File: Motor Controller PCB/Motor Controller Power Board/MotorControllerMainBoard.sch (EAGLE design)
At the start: 58 parts, among them U1 CDBA340L-G

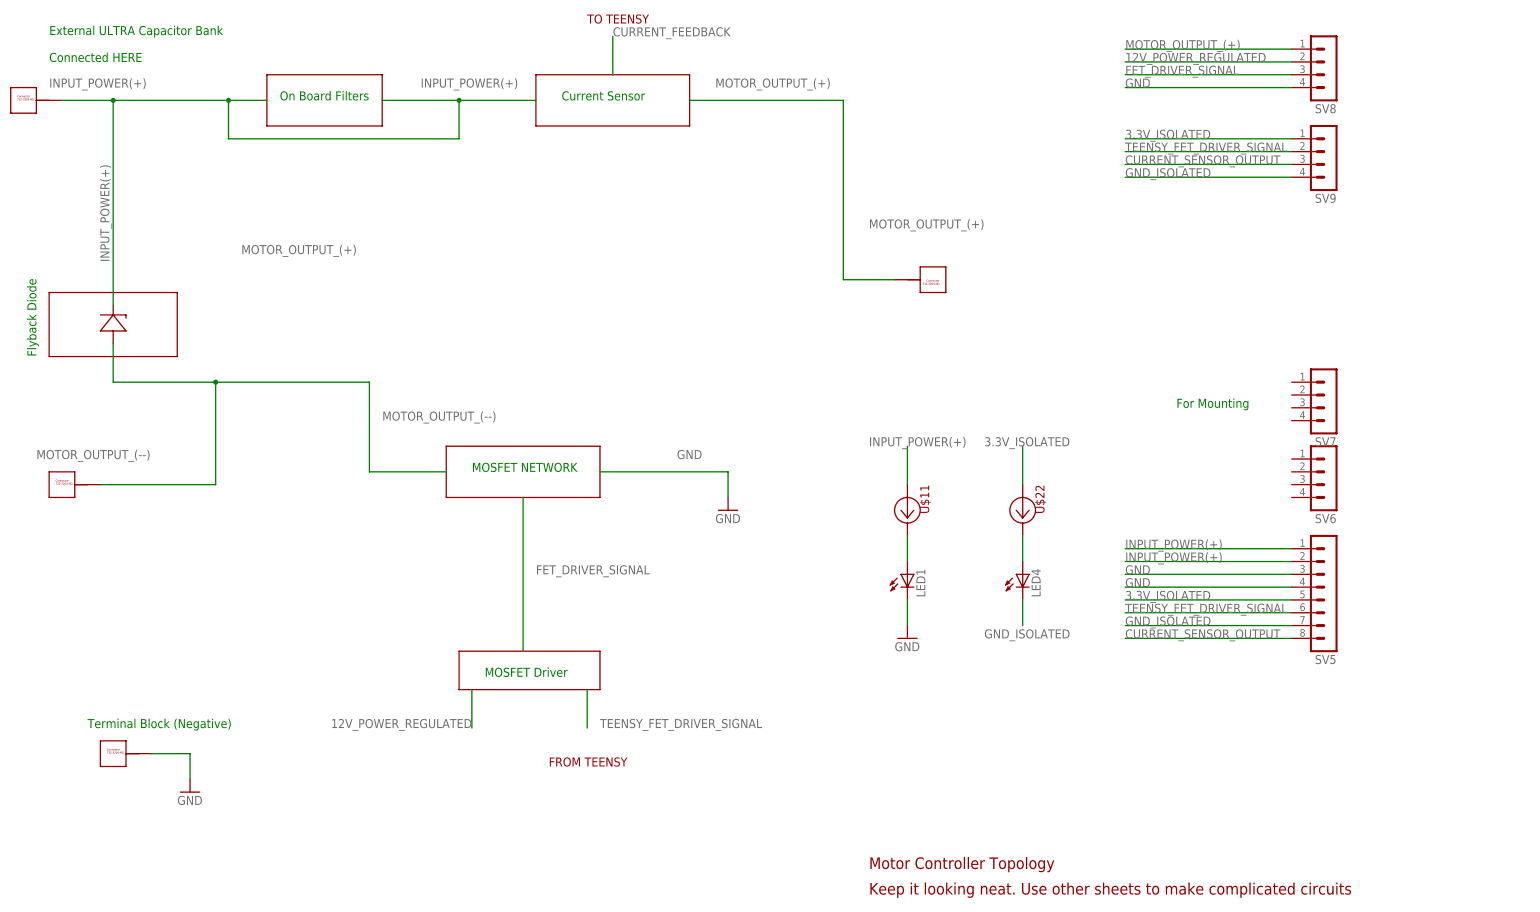
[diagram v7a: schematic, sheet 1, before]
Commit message: added heatsink for flyback diode
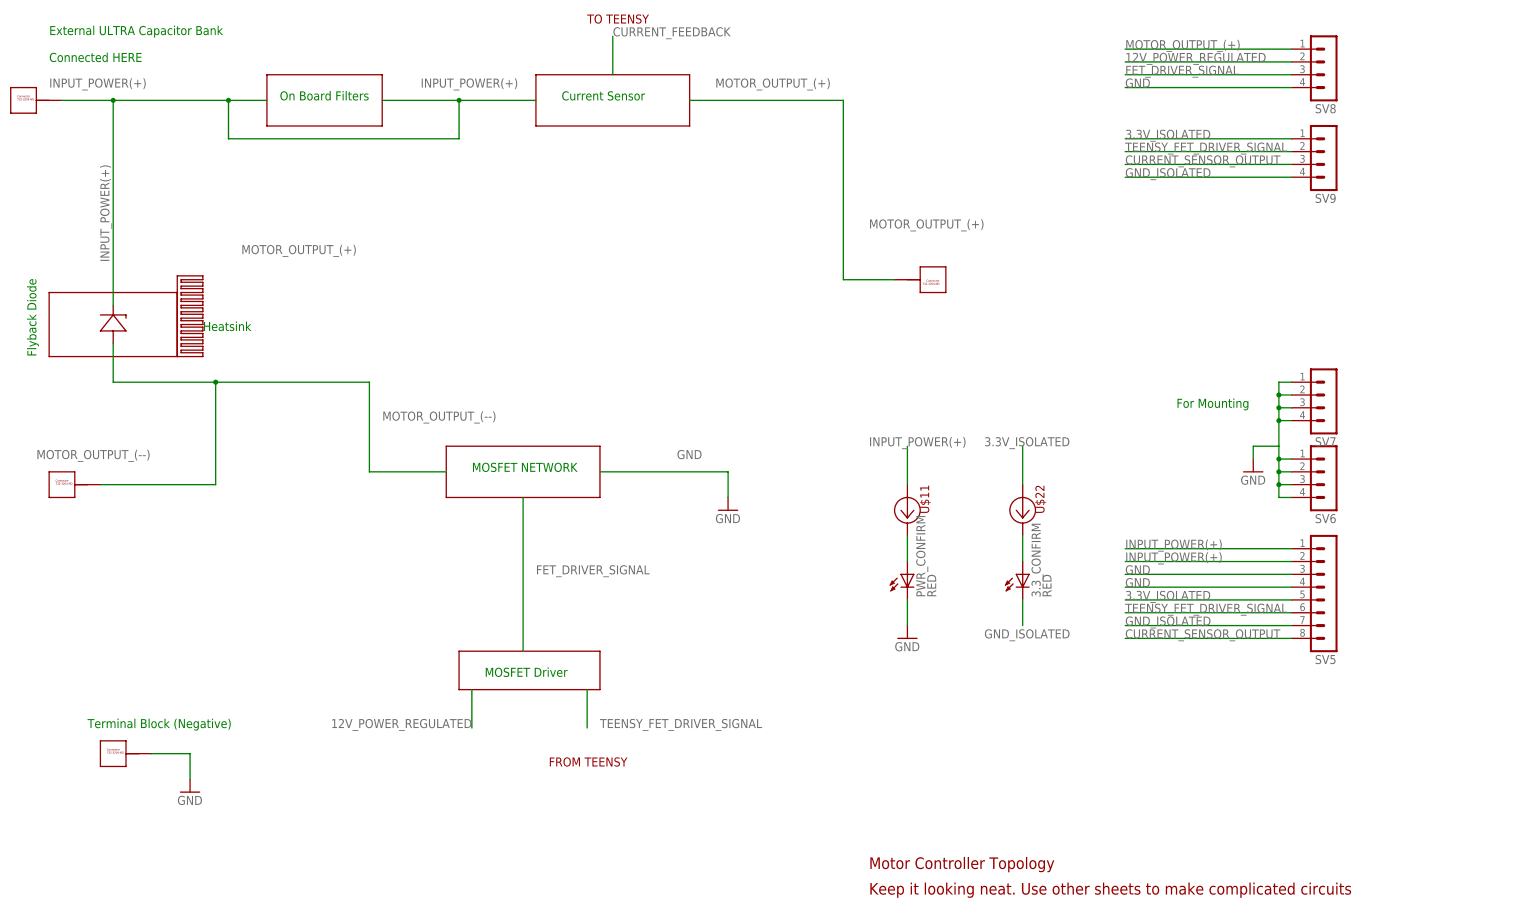
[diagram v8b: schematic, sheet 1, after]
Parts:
- added U$23: DA-T263-101E, MotorControllerEagleLibrary:DA-T263-101E
- 3.3_CONFIRM, PWR_CONFIRM: value (none) -> RED
- renumbered LED1 to PWR_CONFIRM, LED4 to 3.3_CONFIRM
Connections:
- net GND: now also SV6.1, SV6.2, SV6.3, SV6.4, SV7.1, SV7.2, SV7.3, SV7.4
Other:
- note added: "Heatsink"
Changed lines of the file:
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@@
 <?xml version="1.0" encoding="utf-8"?>
 <!DOCTYPE eagle SYSTEM "eagle.dtd">
-<eagle version="8.4.0">
+<eagle version="8.6.0">
 <drawing>
 <settings>
@@
 <part name="C8" library="MotorControllerEagleLibrary" deviceset="EEUFR1H221B" device=""/>
 <part name="U$11" library="MotorControllerEagleLibrary" deviceset="AL5809-20S1-7" device=""/>
-<part name="LED1" library="led" library_urn="urn:adsk.eagle:library:259" deviceset="LED" device="CHIPLED_1206" package3d_urn="urn:adsk.eagle:package:15823/1"/>
+<part name="PWR_CONFIRM" library="led" library_urn="urn:adsk.eagle:library:259" deviceset="LED" device="CHIPLED_1206" package3d_urn="urn:adsk.eagle:package:15823/2" value="RED"/>
 <part name="GND22" library="E-P-008-R1.2" deviceset="GND" device=""/>
 <part name="U$10" library="MotorControllerEagleLibrary" deviceset="EEU-FM1H102B" device=""/>
@@
 <part name="SV9" library="con-lstb" library_urn="urn:adsk.eagle:library:162" deviceset="MA04-1" device="" package3d_urn="urn:adsk.eagle:package:8337/1"/>
 <part name="U$22" library="MotorControllerEagleLibrary" deviceset="AL5809-20S1-7" device=""/>
-<part name="LED4" library="led" library_urn="urn:adsk.eagle:library:259" deviceset="LED" device="CHIPLED_1206" package3d_urn="urn:adsk.eagle:package:15823/1"/>
+<part name="3.3_CONFIRM" library="led" library_urn="urn:adsk.eagle:library:259" deviceset="LED" device="CHIPLED_1206" package3d_urn="urn:adsk.eagle:package:15823/2" value="RED"/>
+<part name="GND10" library="E-P-008-R1.2" deviceset="GND" device=""/>
+<part name="U$23" library="MotorControllerEagleLibrary" deviceset="DA-T263-101E" device=""/>
 </parts>
 <sheets>
@@
 <text x="20.32" y="58.42" size="1.778" layer="91">Terminal Block (Negative)</text>
 <text x="236.22" y="121.92" size="1.778" layer="91">For Mounting</text>
+<text x="43.18" y="137.16" size="1.778" layer="91">Heatsink</text>
 </plain>
 <instances>
@@
 <instance part="U$16" gate="G$1" x="15.24" y="106.68"/>
 <instance part="U$11" gate="G$1" x="182.88" y="101.6" rot="R180"/>
-<instance part="LED1" gate="G$1" x="182.88" y="88.9"/>
+<instance part="PWR_CONFIRM" gate="G$1" x="182.88" y="88.9"/>
 <instance part="GND22" gate="1" x="182.88" y="76.2"/>
 <instance part="SV5" gate="1" x="266.7" y="86.36" rot="R180"/>
@@
 <instance part="SV9" gate="1" x="266.7" y="170.18" rot="R180"/>
 <instance part="U$22" gate="G$1" x="205.74" y="101.6" rot="R180"/>
-<instance part="LED4" gate="G$1" x="205.74" y="88.9"/>
+<instance part="3.3_CONFIRM" gate="G$1" x="205.74" y="88.9"/>
+<instance part="GND10" gate="1" x="251.46" y="109.22"/>
+<instance part="U$23" gate="G$1" x="38.1" y="139.7" rot="R270"/>
 </instances>
 <busses>
@@
 </segment>
 <segment>
-<pinref part="LED1" gate="G$1" pin="C"/>
+<pinref part="PWR_CONFIRM" gate="G$1" pin="C"/>
 <wire x1="182.88" y1="83.82" x2="182.88" y2="78.74" width="0.1524" layer="91"/>
 <pinref part="GND22" gate="1" pin="GND"/>
@@
 <wire x1="259.08" y1="185.42" x2="226.06" y2="185.42" width="0.1524" layer="91"/>
 <label x="226.06" y="185.42" size="1.778" layer="95"/>
+</segment>
+<segment>
+<pinref part="SV7" gate="1" pin="1"/>
+<wire x1="259.08" y1="127" x2="256.54" y2="127" width="0.1524" layer="91"/>
+<wire x1="256.54" y1="127" x2="256.54" y2="124.46" width="0.1524" layer="91"/>
+<pinref part="SV7" gate="1" pin="4"/>
+<wire x1="256.54" y1="124.46" x2="256.54" y2="121.92" width="0.1524" layer="91"/>
+<wire x1="256.54" y1="121.92" x2="256.54" y2="119.38" width="0.1524" layer="91"/>
+<wire x1="256.54" y1="119.38" x2="259.08" y2="119.38" width="0.1524" layer="91"/>
+<pinref part="SV7" gate="1" pin="2"/>
+<wire x1="259.08" y1="124.46" x2="256.54" y2="124.46" width="0.1524" layer="91"/>
+<junction x="256.54" y="124.46"/>
+<pinref part="SV7" gate="1" pin="3"/>
+<wire x1="259.08" y1="121.92" x2="256.54" y2="121.92" width="0.1524" layer="91"/>
+<junction x="256.54" y="121.92"/>
+<pinref part="SV6" gate="1" pin="1"/>
+<wire x1="259.08" y1="111.76" x2="256.54" y2="111.76" width="0.1524" layer="91"/>
+<pinref part="SV6" gate="1" pin="4"/>
+<wire x1="256.54" y1="111.76" x2="256.54" y2="109.22" width="0.1524" layer="91"/>
+<wire x1="256.54" y1="109.22" x2="256.54" y2="106.68" width="0.1524" layer="91"/>
+<wire x1="256.54" y1="106.68" x2="256.54" y2="104.14" width="0.1524" layer="91"/>
+<wire x1="256.54" y1="104.14" x2="259.08" y2="104.14" width="0.1524" layer="91"/>
+<pinref part="SV6" gate="1" pin="3"/>
+<wire x1="259.08" y1="106.68" x2="256.54" y2="106.68" width="0.1524" layer="91"/>
+<junction x="256.54" y="106.68"/>
+<pinref part="SV6" gate="1" pin="2"/>
+<wire x1="259.08" y1="109.22" x2="256.54" y2="109.22" width="0.1524" layer="91"/>
+<junction x="256.54" y="109.22"/>
+<junction x="256.54" y="119.38"/>
+<junction x="256.54" y="111.76"/>
+<wire x1="256.54" y1="114.3" x2="256.54" y2="111.76" width="0.1524" layer="91"/>
+<wire x1="256.54" y1="119.38" x2="256.54" y2="114.3" width="0.1524" layer="91"/>
+<wire x1="256.54" y1="114.3" x2="251.46" y2="114.3" width="0.1524" layer="91"/>
+<pinref part="GND10" gate="1" pin="GND"/>
+<wire x1="251.46" y1="114.3" x2="251.46" y2="111.76" width="0.1524" layer="91"/>
 </segment>
 </net>
@@
 <segment>
 <pinref part="U$11" gate="G$1" pin="C"/>
-<pinref part="LED1" gate="G$1" pin="A"/>
+<pinref part="PWR_CONFIRM" gate="G$1" pin="A"/>
 <wire x1="182.88" y1="96.52" x2="182.88" y2="91.44" width="0.1524" layer="91"/>
 </segment>
@@
 </segment>
 <segment>
-<pinref part="LED4" gate="G$1" pin="C"/>
+<pinref part="3.3_CONFIRM" gate="G$1" pin="C"/>
 <wire x1="205.74" y1="83.82" x2="205.74" y2="78.74" width="0.1524" layer="91"/>
 <label x="198.12" y="76.2" size="1.778" layer="95"/>
@@
 <segment>
 <pinref part="U$22" gate="G$1" pin="C"/>
-<pinref part="LED4" gate="G$1" pin="A"/>
+<pinref part="3.3_CONFIRM" gate="G$1" pin="A"/>
 <wire x1="205.74" y1="96.52" x2="205.74" y2="91.44" width="0.1524" layer="91"/>
 </segment>
@@
 packages will not be understood (or retained) with this version.
 </note>
+<note version="8.4" severity="warning">
+Since Version 8.4, EAGLE supports properties for SPICE simulation.
+Probes in schematics and SPICE mapping objects found in parts and library devices
+will not be understood with this version. Update EAGLE to the latest version
+for full support of SPICE simulation.
+</note>
 </compatibility>
